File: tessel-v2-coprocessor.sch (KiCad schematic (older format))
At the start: 42 parts, among them J401 CONN_02X05, J402 USB-micro-TH, J403 MODULE_HEADER, J404 MODULE_HEADER, J405 CONN_01X01, SW401 SW_PUSH, U401 SAMD21G14A-MU, X401 FC-135

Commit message: moving to intrernal RLC symbols...~half way there, by sheets
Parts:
- C401, C402, C403, C404, C405, C406, C407, C408, C409, C410, C411: symbol C -> TM_C
- L401: symbol INDUCTOR -> TM_L
- R401, R402, R403, R404, R405, R406, R407, R408, R409, R410, R411, R412, R413, R414, R415, R416, R417, R418, R419, R420: symbol R -> TM_R
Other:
- moved on the sheet: D402

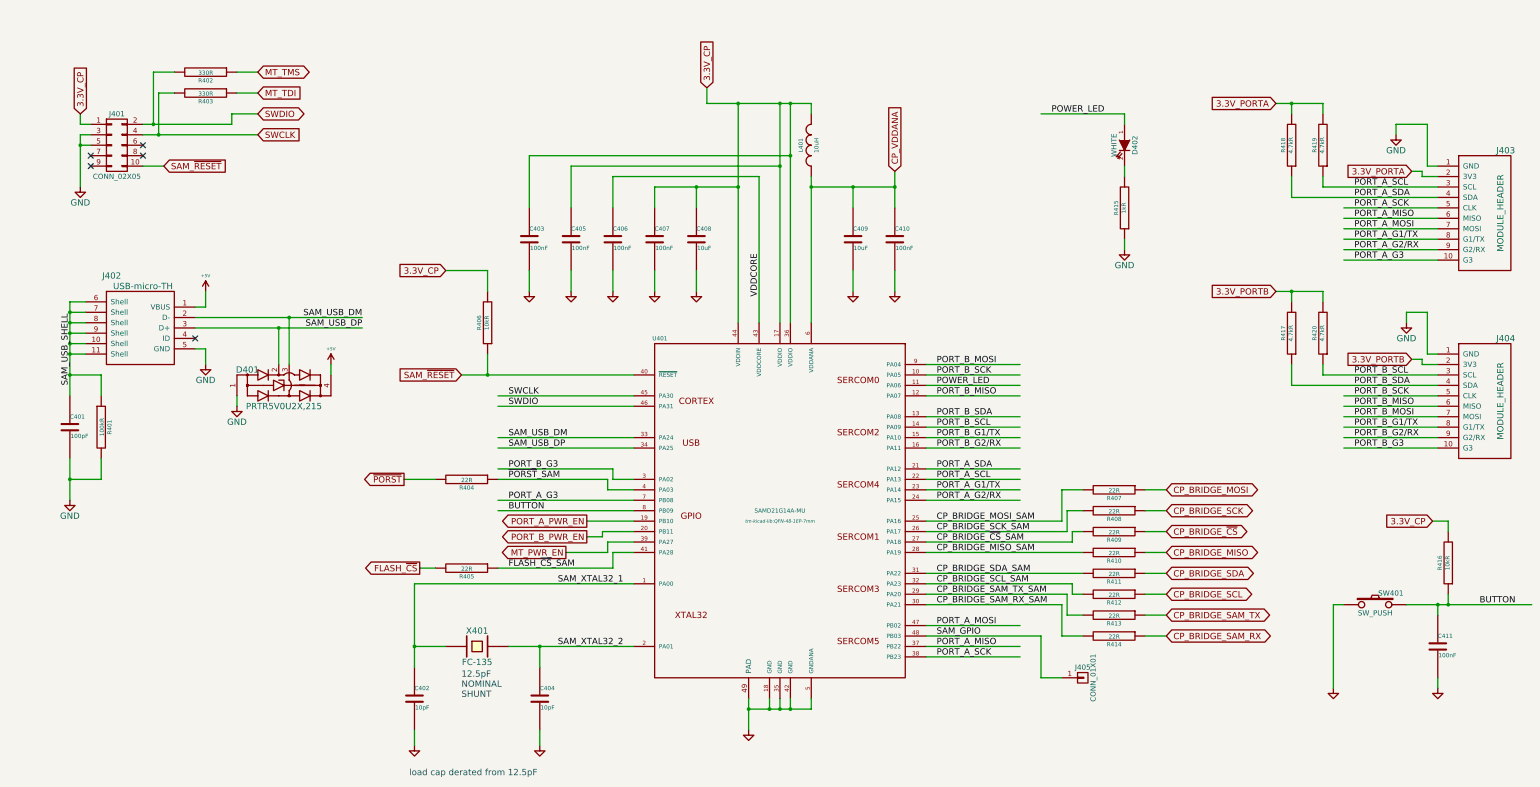
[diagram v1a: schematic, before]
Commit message: swapped out all RLCs
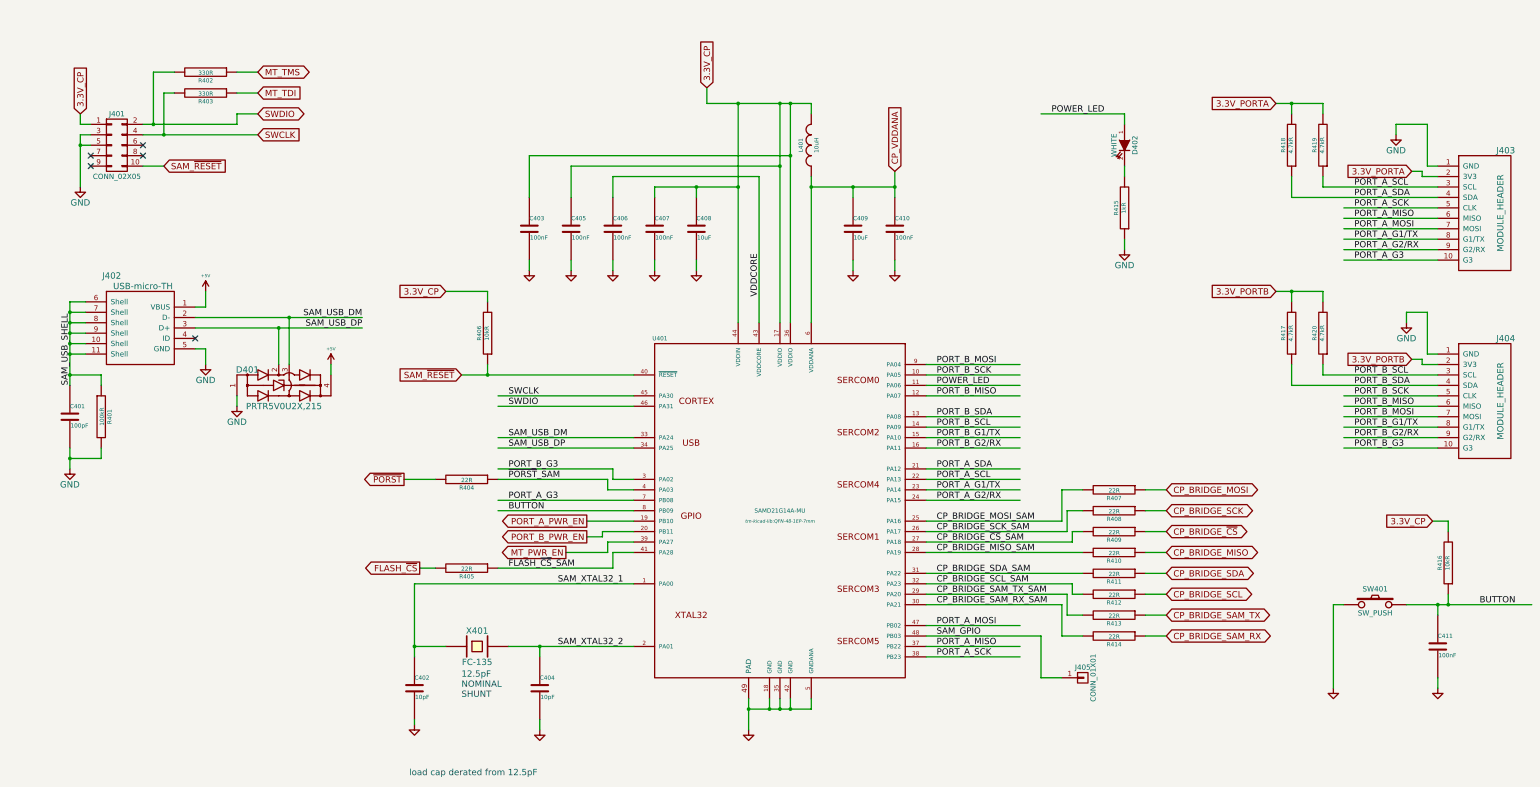
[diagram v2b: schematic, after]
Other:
- moved on the sheet: C401, C402, C403, C404, C405, C406, C407, C408, C409, C410, R401, R406

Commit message: project save
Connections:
- wire segments 239 -> 204
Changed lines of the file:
@@
 $EndComp
 $Comp
-L GND #PWR407
+L GND #PWR0110
 U 1 1 548F9730
 P 4800 8050
-F 0 "#PWR407" H 4800 8050 30  0001 C CNN
+F 0 "#PWR0110" H 4800 8050 30  0001 C CNN
 F 1 "GND" H 4800 7980 30  0001 C CNN
 F 2 "" H 4800 8050 60  0000 C CNN
@@
 $EndComp
 $Comp
-L GND #PWR409
+L GND #PWR0111
 U 1 1 548F973F
 P 6000 8100
-F 0 "#PWR409" H 6000 8100 30  0001 C CNN
+F 0 "#PWR0111" H 6000 8100 30  0001 C CNN
 F 1 "GND" H 6000 8030 30  0001 C CNN
 F 2 "" H 6000 8100 60  0000 C CNN
@@
 VDDCORE
 $Comp
-L GND #PWR416
+L GND #PWR0112
 U 1 1 548FA205
 P 9400 3700
-F 0 "#PWR416" H 9400 3700 30  0001 C CNN
+F 0 "#PWR0112" H 9400 3700 30  0001 C CNN
 F 1 "GND" H 9400 3630 30  0001 C CNN
 F 2 "" H 9400 3700 60  0000 C CNN
@@
 $EndComp
 $Comp
-L GND #PWR415
+L GND #PWR0113
 U 1 1 548FBD70
 P 9000 3700
-F 0 "#PWR415" H 9000 3700 30  0001 C CNN
+F 0 "#PWR0113" H 9000 3700 30  0001 C CNN
 F 1 "GND" H 9000 3630 30  0001 C CNN
 F 2 "" H 9000 3700 60  0000 C CNN
@@
 $EndComp
 $Comp
-L GND #PWR413
+L GND #PWR0114
 U 1 1 548FBD83
 P 7500 3700
-F 0 "#PWR413" H 7500 3700 30  0001 C CNN
+F 0 "#PWR0114" H 7500 3700 30  0001 C CNN
 F 1 "GND" H 7500 3630 30  0001 C CNN
 F 2 "" H 7500 3700 60  0000 C CNN
@@
 $EndComp
 $Comp
-L GND #PWR412
+L GND #PWR0115
 U 1 1 548FBD8A
 P 7100 3700
-F 0 "#PWR412" H 7100 3700 30  0001 C CNN
+F 0 "#PWR0115" H 7100 3700 30  0001 C CNN
 F 1 "GND" H 7100 3630 30  0001 C CNN
 F 2 "" H 7100 3700 60  0000 C CNN
@@
 $EndComp
 $Comp
-L GND #PWR411
+L GND #PWR0116
 U 1 1 548FBD9D
 P 6700 3700
-F 0 "#PWR411" H 6700 3700 30  0001 C CNN
+F 0 "#PWR0116" H 6700 3700 30  0001 C CNN
 F 1 "GND" H 6700 3630 30  0001 C CNN
 F 2 "" H 6700 3700 60  0000 C CNN
@@
 $EndComp
 $Comp
-L GND #PWR410
+L GND #PWR0117
 U 1 1 548FBDA4
 P 6300 3700
-F 0 "#PWR410" H 6300 3700 30  0001 C CNN
+F 0 "#PWR0117" H 6300 3700 30  0001 C CNN
 F 1 "GND" H 6300 3630 30  0001 C CNN
 F 2 "" H 6300 3700 60  0000 C CNN
@@
 $EndComp
 $Comp
-L GND #PWR408
+L GND #PWR0118
 U 1 1 548FBDB7
 P 5900 3700
-F 0 "#PWR408" H 5900 3700 30  0001 C CNN
+F 0 "#PWR0118" H 5900 3700 30  0001 C CNN
 F 1 "GND" H 5900 3630 30  0001 C CNN
 F 2 "" H 5900 3700 60  0000 C CNN
@@
 $EndComp
 $Comp
-L GND #PWR414
+L GND #PWR0119
 U 1 1 548FD791
 P 8000 8100
-F 0 "#PWR414" H 8000 8100 30  0001 C CNN
+F 0 "#PWR0119" H 8000 8100 30  0001 C CNN
 F 1 "GND" H 8000 8030 30  0001 C CNN
 F 2 "" H 8000 8100 60  0000 C CNN
@@
 $EndComp
 $Comp
-L GND #PWR421
+L GND #PWR0120
 U 1 1 54E6B173
 P 14600 7700
-F 0 "#PWR421" H 14600 7700 30  0001 C CNN
+F 0 "#PWR0120" H 14600 7700 30  0001 C CNN
 F 1 "GND" H 14600 7630 30  0001 C CNN
 F 2 "" H 14600 7700 60  0000 C CNN
@@
 3.3V_CP
 $Comp
-L GND #PWR418
+L GND #PWR0121
 U 1 1 54E6B4A0
 P 13600 7700
-F 0 "#PWR418" H 13600 7700 30  0001 C CNN
+F 0 "#PWR0121" H 13600 7700 30  0001 C CNN
 F 1 "GND" H 13600 7630 30  0001 C CNN
 F 2 "" H 13600 7700 60  0000 C CNN
@@
 NoConn ~ 1700 2700
 $Comp
-L GND #PWR402
+L GND #PWR0122
 U 1 1 54E6D866
 P 1600 2900
-F 0 "#PWR402" H 1600 2650 60  0001 C CNN
+F 0 "#PWR0122" H 1600 2650 60  0001 C CNN
 F 1 "GND" H 1600 2750 60  0000 C CNN
 F 2 "" H 1600 2900 60  0000 C CNN
@@
 3.3V_PORTA
 $Comp
-L GND #PWR419
+L GND #PWR0123
 U 1 1 54E753B7
 P 14200 2400
-F 0 "#PWR419" H 14200 2150 60  0001 C CNN
+F 0 "#PWR0123" H 14200 2150 60  0001 C CNN
 F 1 "GND" H 14200 2250 60  0000 C CNN
 F 2 "" H 14200 2400 60  0000 C CNN
@@
 $EndComp
 $Comp
-L GND #PWR420
+L GND #PWR0124
 U 1 1 54E753CD
 P 14300 4200
-F 0 "#PWR420" H 14300 3950 60  0001 C CNN
+F 0 "#PWR0124" H 14300 3950 60  0001 C CNN
 F 1 "GND" H 14300 4050 60  0000 C CNN
 F 2 "" H 14300 4200 60  0000 C CNN
@@
 PORT_A_G3
 $Comp
-L +5V #PWR403
+L +5V #PWR0125
 U 1 1 54E79A0D
 P 2800 3900
-F 0 "#PWR403" H 2800 3990 20  0001 C CNN
+F 0 "#PWR0125" H 2800 3990 20  0001 C CNN
 F 1 "+5V" H 2800 4050 30  0000 C CNN
 F 2 "" H 2800 3900 60  0000 C CNN
@@
 $EndComp
 $Comp
-L GND #PWR404
+L GND #PWR0126
 U 1 1 54E79A13
 P 2800 4600
-F 0 "#PWR404" H 2800 4350 60  0001 C CNN
+F 0 "#PWR0126" H 2800 4350 60  0001 C CNN
 F 1 "GND" H 2800 4450 60  0000 C CNN
 F 2 "" H 2800 4600 60  0000 C CNN
@@
 $EndComp
 $Comp
-L GND #PWR405
+L GND #PWR0127
 U 1 1 54E79A19
 P 3100 5000
-F 0 "#PWR405" H 3100 4750 60  0001 C CNN
+F 0 "#PWR0127" H 3100 4750 60  0001 C CNN
 F 1 "GND" H 3100 4850 60  0000 C CNN
 F 2 "" H 3100 5000 60  0000 C CNN
@@
 $EndComp
 $Comp
-L GND #PWR401
+L GND #PWR0128
 U 1 1 54E79A1F
 P 1500 5600
-F 0 "#PWR401" H 1500 5350 60  0001 C CNN
+F 0 "#PWR0128" H 1500 5350 60  0001 C CNN
 F 1 "GND" H 1500 5450 60  0000 C CNN
 F 2 "" H 1500 5600 60  0000 C CNN
@@
 $EndComp
 $Comp
-L +5V #PWR406
+L +5V #PWR0129
 U 1 1 54E79A2D
 P 4000 4600
-F 0 "#PWR406" H 4000 4690 20  0001 C CNN
+F 0 "#PWR0129" H 4000 4690 20  0001 C CNN
 F 1 "+5V" H 4000 4750 30  0000 C CNN
 F 2 "" H 4000 4600 60  0000 C CNN
@@
 FLASH_~CS
 $Comp
-L GND #PWR417
+L GND #PWR0130
 U 1 1 54EE1D18
 P 11600 3500
-F 0 "#PWR417" H 11600 3250 60  0001 C CNN
+F 0 "#PWR0130" H 11600 3250 60  0001 C CNN
 F 1 "GND" H 11600 3350 60  0000 C CNN
 F 2 "" H 11600 3500 60  0000 C CNN
@@
 	1800 5400 1800 5500
 Wire Wire Line
-	1500 5400 1500 5500
-Wire Wire Line
-	1500 5500 1500 5600
-Wire Wire Line
-	1500 4000 1500 4100
-Wire Wire Line
-	1500 4100 1500 4200
-Wire Wire Line
-	1500 4200 1500 4300
-Wire Wire Line
-	1500 4300 1500 4400
-Wire Wire Line
-	1500 4400 1500 4500
-Wire Wire Line
-	1500 4500 1500 4700
-Wire Wire Line
-	1500 4700 1500 4800
+	1500 5400 1500 5600
+Wire Wire Line
+	1500 4000 1500 4800
 Wire Wire Line
 	1800 4700 1500 4700
@@
 Connection ~ 3500 4250
 Wire Wire Line
-	2700 4250 3500 4250
-Wire Wire Line
-	3500 4250 4300 4250
-Wire Wire Line
-	2700 4150 3600 4150
-Wire Wire Line
-	3600 4150 4300 4150
+	2700 4250 4300 4250
+Wire Wire Line
+	2700 4150 4300 4150
 Wire Wire Line
 	2700 4050 2800 4050
@@
 	1600 2300 1600 2200
 Wire Wire Line
-	2200 2300 2300 2300
-Wire Wire Line
-	2300 2300 3100 2300
-Wire Wire Line
-	2200 2400 2400 2400
-Wire Wire Line
-	2400 2400 3300 2400
+	2200 2300 3100 2300
+Wire Wire Line
+	2200 2400 3300 2400
 Wire Wire Line
 	2400 2700 2200 2700
@@
 	1700 2400 1600 2400
 Wire Wire Line
-	1600 2400 1600 2500
-Wire Wire Line
-	1600 2500 1600 2900
+	1600 2400 1600 2900
 Wire Wire Line
 	1700 2500 1600 2500
@@
 	14700 6900 14700 6800
 Wire Wire Line
-	14300 6900 14600 6900
-Wire Wire Line
-	14600 6900 14700 6900
-Wire Wire Line
-	14700 6900 15500 6900
+	14300 6900 15500 6900
 Wire Wire Line
 	14550 6100 14700 6100
@@
 	8200 7900 8200 7800
 Wire Wire Line
-	8000 7900 8200 7900
-Wire Wire Line
-	8200 7900 8300 7900
-Wire Wire Line
-	8300 7900 8400 7900
-Wire Wire Line
-	8400 7900 8600 7900
-Wire Wire Line
-	8000 7800 8000 7900
-Wire Wire Line
-	8000 7900 8000 8100
+	8000 7900 8600 7900
+Wire Wire Line
+	8000 7800 8000 8100
 Connection ~ 7500 2900
 Wire Wire Line
 	7500 3000 7500 2900
 Wire Wire Line
-	7600 2100 7900 2100
-Wire Wire Line
-	7900 2100 8300 2100
-Wire Wire Line
-	8300 2100 8400 2100
-Wire Wire Line
-	8400 2100 8600 2100
-Wire Wire Line
-	5250 4700 5500 4700
-Wire Wire Line
-	5500 4700 6900 4700
+	7600 2100 8600 2100
+Wire Wire Line
+	5250 4700 6900 4700
 Wire Wire Line
 	6900 4900 5600 4900
@@
 	4800 6700 6900 6700
 Wire Wire Line
-	5700 7300 6000 7300
-Wire Wire Line
-	6000 7300 6900 7300
+	5700 7300 6900 7300
 Wire Wire Line
 	9700 4600 10600 4600
@@
 	9700 7100 10600 7100
 Wire Wire Line
-	4800 6700 4800 7300
-Wire Wire Line
-	4800 7300 4800 7400
+	4800 6700 4800 7400
 Wire Wire Line
 	4800 7300 5100 7300
@@
 	4800 8000 4800 8050
 Wire Wire Line
-	8600 2800 8600 2900
-Wire Wire Line
-	8600 2900 8600 4200
-Wire Wire Line
-	8600 2900 9000 2900
-Wire Wire Line
-	9000 2900 9400 2900
+	8600 2800 8600 4200
+Wire Wire Line
+	8600 2900 9400 2900
 Wire Wire Line
 	9000 2900 9000 3000
 Wire Wire Line
-	9400 2750 9400 2900
-Wire Wire Line
-	9400 2900 9400 3000
+	9400 2750 9400 3000
 Connection ~ 9000 2900
 Connection ~ 8600 2900
 Wire Wire Line
-	7100 2900 7500 2900
-Wire Wire Line
-	7500 2900 7900 2900
+	7100 2900 7900 2900
 Wire Wire Line
 	7100 2900 7100 3000
@@
 	8100 2800 8100 4200
 Wire Wire Line
-	8300 2100 8300 2700
-Wire Wire Line
-	8300 2700 8300 4200
+	8300 2100 8300 4200
 Wire Wire Line
 	8300 2700 6300 2700
@@
 	7600 2100 7600 1950
 Wire Wire Line
-	8400 2100 8400 2600
-Wire Wire Line
-	8400 2600 8400 4200
+	8400 2100 8400 4200
 Connection ~ 8400 2100
 Connection ~ 8400 2600
@@
 Connection ~ 8300 2700
 Wire Wire Line
-	7900 2100 7900 2900
-Wire Wire Line
-	7900 2900 7900 4200
+	7900 2100 7900 4200
 Connection ~ 7900 2100
 Connection ~ 7900 2900
@@
 	10800 7600 11000 7600
 Wire Wire Line
-	13200 2100 13500 2100
-Wire Wire Line
-	13200 2100 13200 2100
+	13050 2100 13500 2100
 Wire Wire Line
 	13200 2100 13200 2200
 Text GLabel 13050 2100 0    60   Input ~ 0
 3.3V_PORTA
-Wire Wire Line
-	13050 2100 13200 2100
 Connection ~ 13200 2100
 $Comp
@@
 3.3V_PORTB
 Wire Wire Line
-	13050 3900 13200 3900
-Wire Wire Line
-	13200 3900 13200 3900
+	13050 3900 13500 3900
 Wire Wire Line
 	13200 3900 13200 4000
 Connection ~ 13200 3900
 Wire Wire Line
-	13500 3900 13200 3900
-Wire Wire Line
 	13200 2800 13200 3000

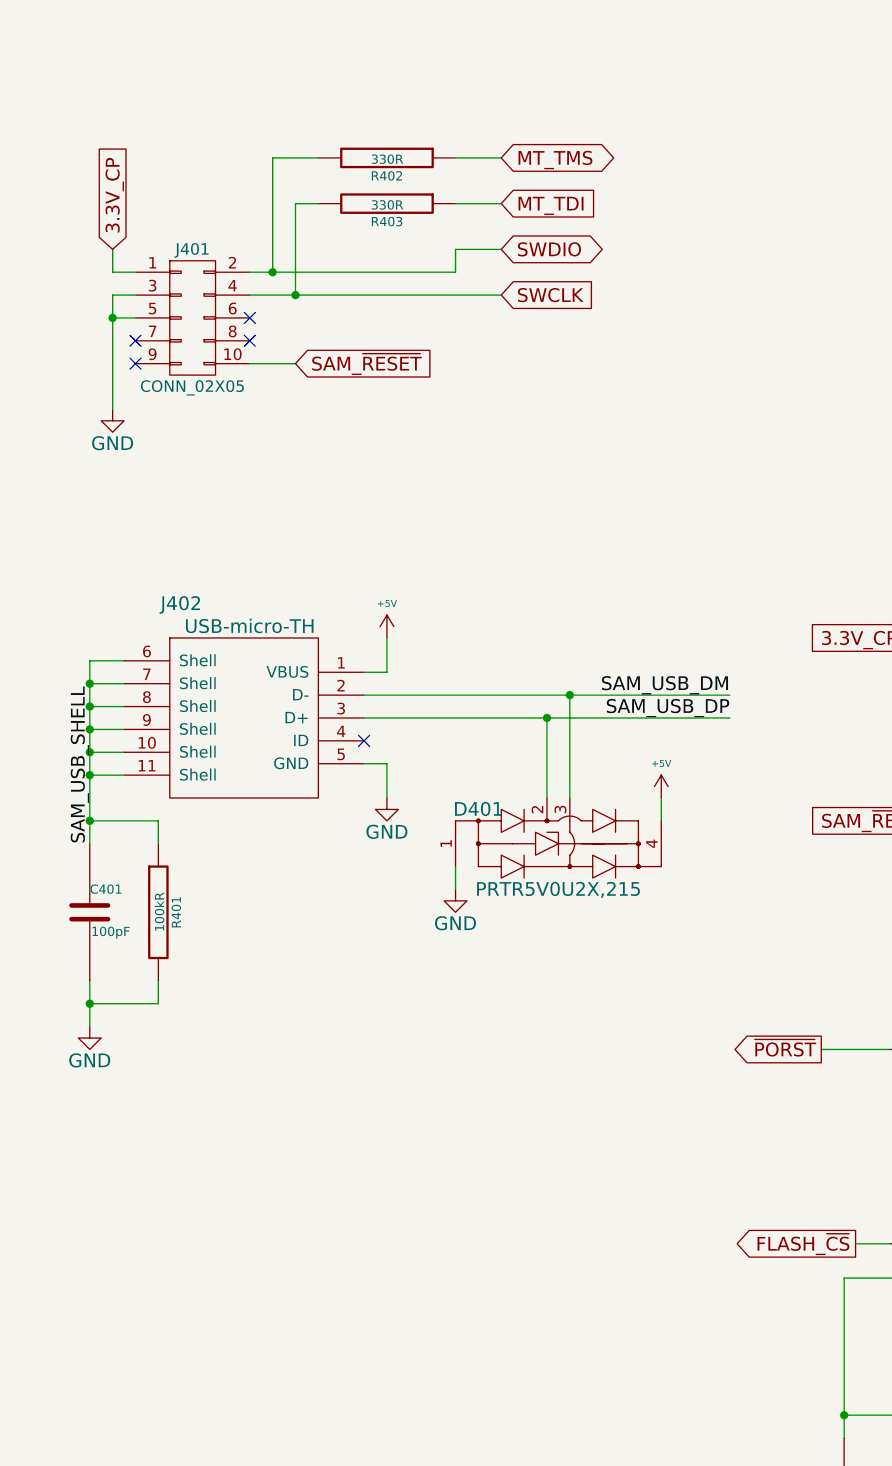
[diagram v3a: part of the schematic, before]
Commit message: added testpoints to swd and power
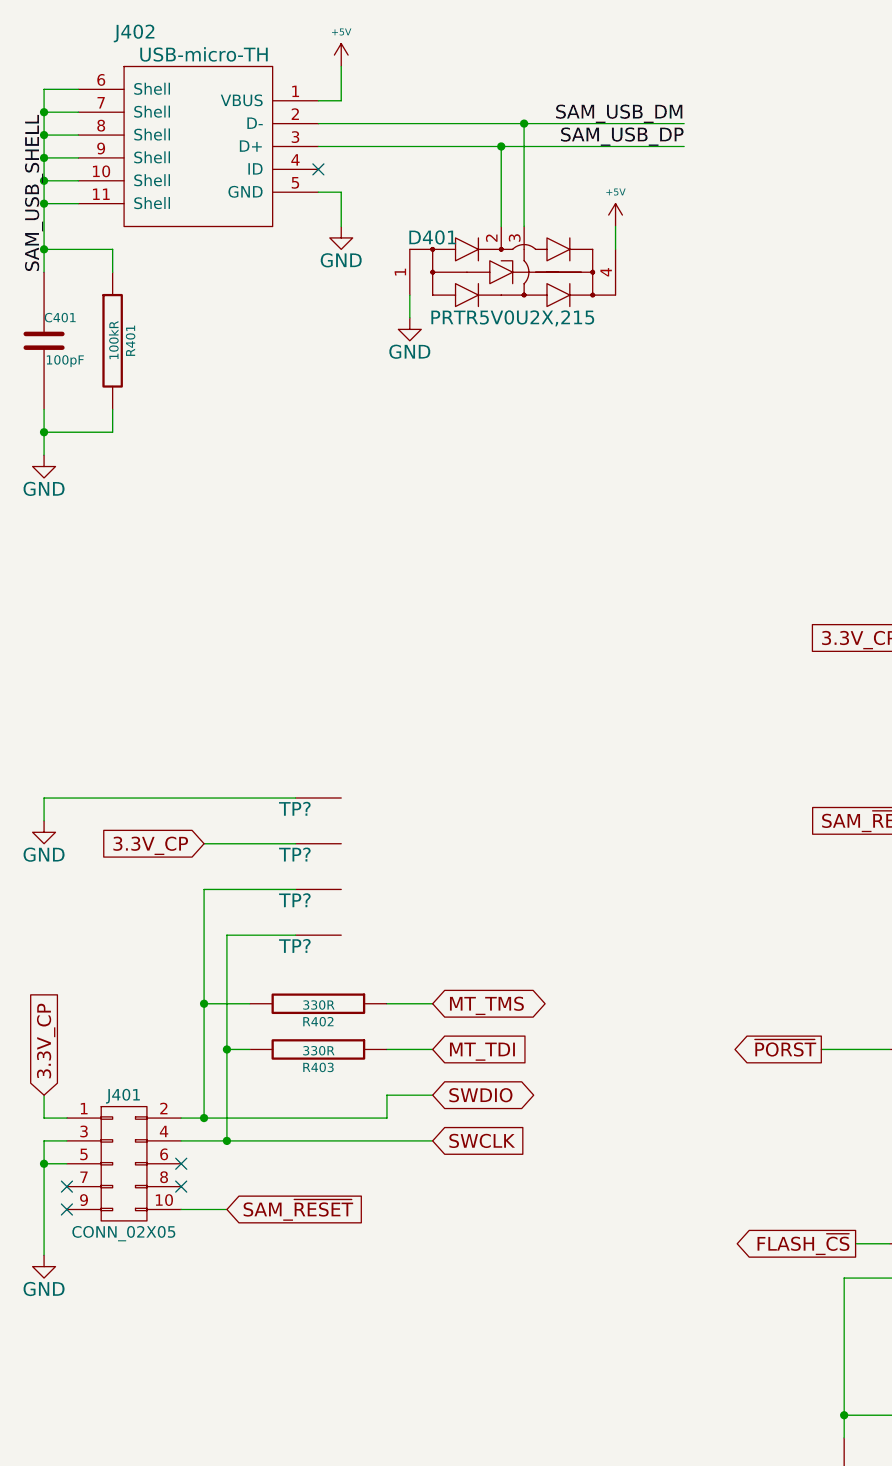
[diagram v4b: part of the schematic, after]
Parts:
- added TP? (x4): TP, symbol TP
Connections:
- wire segments 204 -> 209
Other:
- moved on the sheet: C401, D401, J401, J402, R401, R402, R403
